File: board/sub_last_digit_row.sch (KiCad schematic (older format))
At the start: 55 parts, among them Q801 Q_PMOS_GSD, Q802 Q_PMOS_GSD, Q803 Q_PMOS_GSD, Q804 Q_PMOS_GSD, Q805 Q_PMOS_GSD, Q806 Q_PMOS_GSD, Q807 Q_PMOS_GSD, U801 TPIC6D595, U802 TPIC6D595, U803 TPIC6D595

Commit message: Almost all footprints done
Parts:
- D817, D818, D819: value (none) -> 14-segment; footprint (none) -> quokka:14-segment
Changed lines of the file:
@@
 P 5625 3275
 F 0 "D818" H 4825 3875 50  0000 L CNN
-F 1 " " H 4825 3875 50  0001 L CNN
-F 2 "" V 5225 2925 50  0001 C CNN
+F 1 "14-segment" H 4825 3875 50  0001 L CNN
+F 2 "quokka:14-segment" V 5225 2925 50  0001 C CNN
 F 3 "" V 5225 2925 50  0001 C CNN
 	1    5625 3275
@@
 P 7425 3275
 F 0 "D819" H 6625 3875 50  0000 L CNN
-F 1 " " H 6625 3875 50  0001 L CNN
-F 2 "" V 7025 2925 50  0001 C CNN
+F 1 "14-segment" H 6625 3875 50  0001 L CNN
+F 2 "quokka:14-segment" V 7025 2925 50  0001 C CNN
 F 3 "" V 7025 2925 50  0001 C CNN
 	1    7425 3275
@@
 P 3825 3275
 F 0 "D817" H 3025 3875 50  0000 L CNN
-F 1 " " H 3025 3875 50  0001 L CNN
-F 2 "" V 3425 2925 50  0001 C CNN
+F 1 "14-segment" H 3025 3875 50  0001 L CNN
+F 2 "quokka:14-segment" V 3425 2925 50  0001 C CNN
 F 3 "" V 3425 2925 50  0001 C CNN
 	1    3825 3275

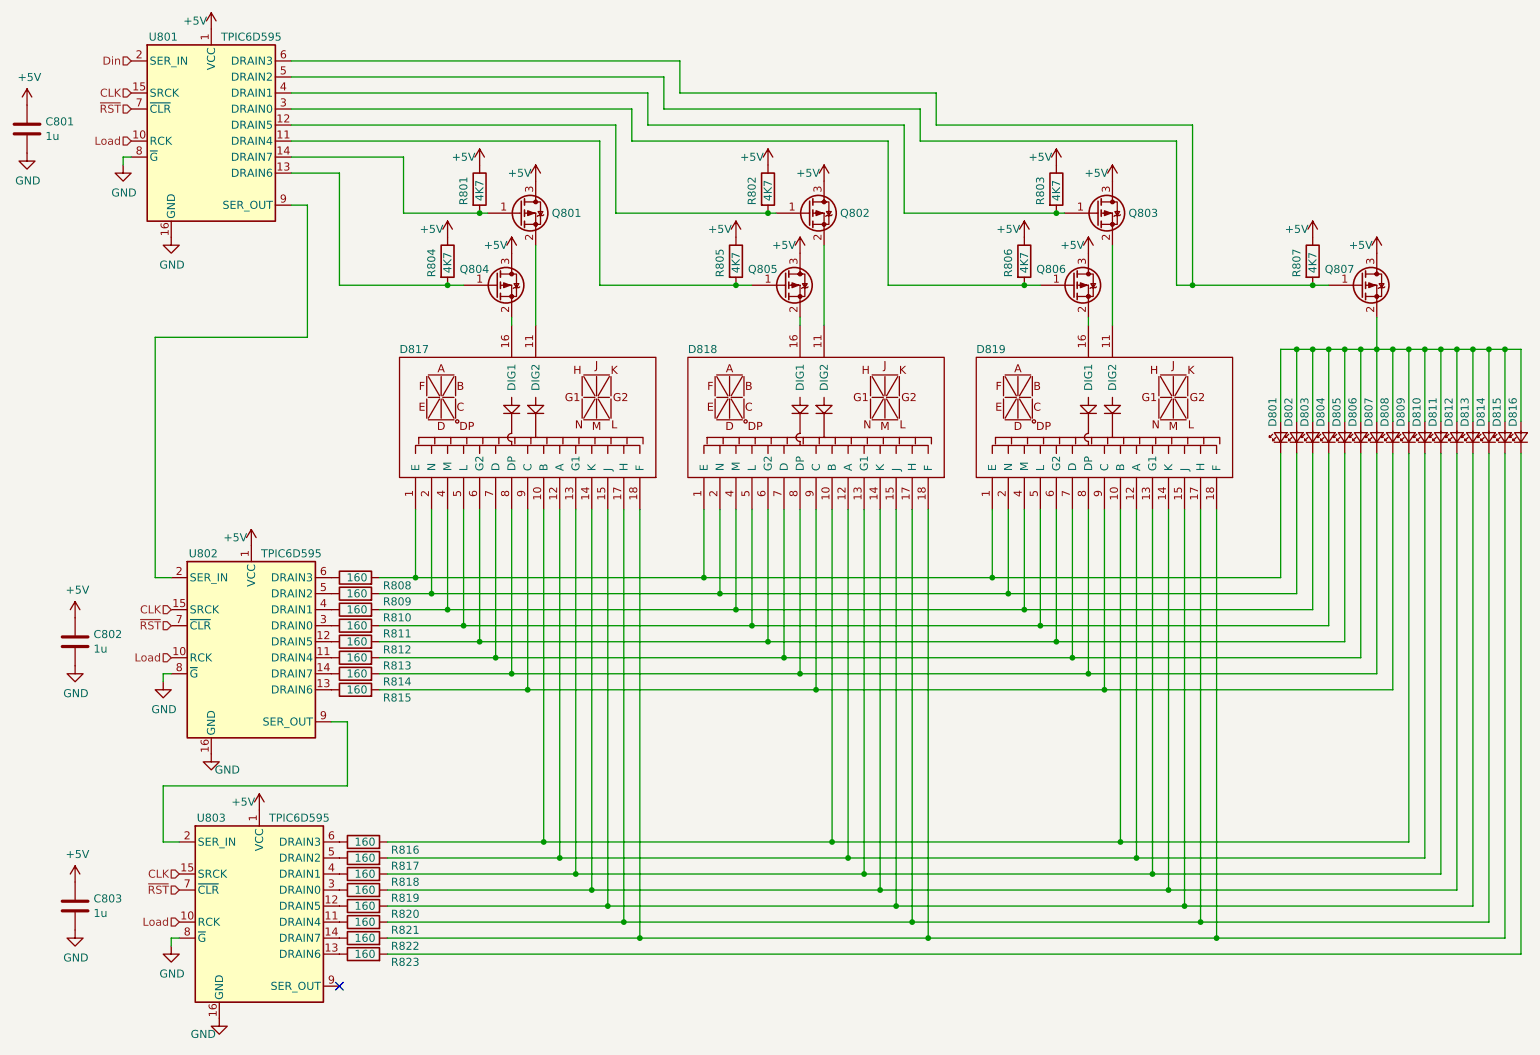
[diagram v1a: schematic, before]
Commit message: Power supply routed
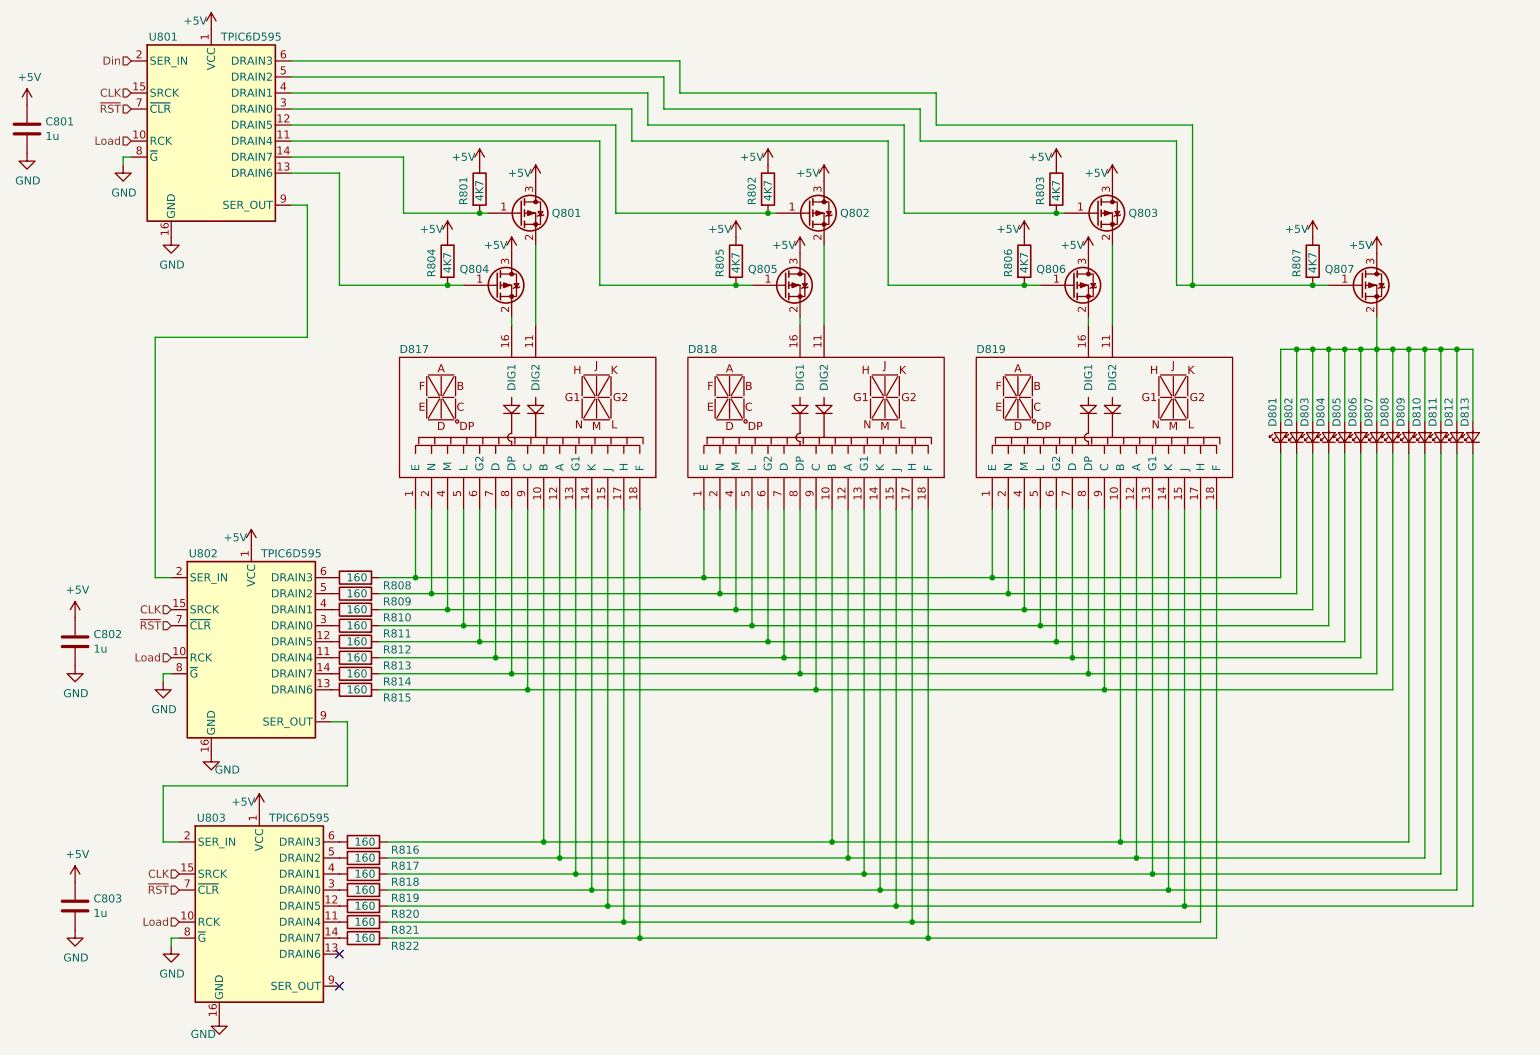
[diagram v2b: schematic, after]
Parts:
- removed D814, D815, D816: LED_Small, LED_SMD:LED_0805_2012Metric, symbol Device:LED_Small
- removed R823: 160, Resistor_SMD:R_1206_3216Metric, symbol Device:R
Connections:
- no-connect marks 1 -> 2
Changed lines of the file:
@@
 $EndComp
-Wire Wire Line
-	9925 2675 9925 3125
-Wire Wire Line
-	9825 2675 9925 2675
-Connection ~ 9825 2675
-Wire Wire Line
-	9825 2675 9825 3125
-Wire Wire Line
-	9725 2675 9825 2675
-Connection ~ 9725 2675
 Wire Wire Line
 	9725 2675 9725 3125
@@
 Wire Wire Line
 	8725 3125 8725 2675
-$Comp
-L Device:LED_Small D815
-U 1 1 5AF22EC2
-P 9925 3225
-F 0 "D815" H 10175 3275 50  0000 R CNN
-F 1 "LED_Small" V 9880 3157 50  0001 R CNN
-F 2 "LED_SMD:LED_0805_2012Metric" V 9925 3225 50  0001 C CNN
-F 3 "~" V 9925 3225 50  0001 C CNN
-	1    9925 3225
-	0    -1   -1   0
-$EndComp
-$Comp
-L Device:LED_Small D814
-U 1 1 5AF22EBC
-P 9825 3225
-F 0 "D814" H 10075 3275 50  0000 R CNN
-F 1 "LED_Small" V 9780 3157 50  0001 R CNN
-F 2 "LED_SMD:LED_0805_2012Metric" V 9825 3225 50  0001 C CNN
-F 3 "~" V 9825 3225 50  0001 C CNN
-	1    9825 3225
-	0    -1   -1   0
-$EndComp
 $Comp
 L Device:LED_Small D813
@@
 	0    -1   -1   0
 $EndComp
-$Comp
-L Device:LED_Small D816
-U 1 1 5AF22EC8
-P 10025 3225
-F 0 "D816" H 10275 3275 50  0000 R CNN
-F 1 "LED_Small" V 9980 3157 50  0001 R CNN
-F 2 "LED_SMD:LED_0805_2012Metric" V 10025 3225 50  0001 C CNN
-F 3 "~" V 10025 3225 50  0001 C CNN
-	1    10025 3225
-	0    -1   -1   0
-$EndComp
-Connection ~ 9925 2675
-Wire Wire Line
-	9925 2675 10025 2675
-Wire Wire Line
-	10025 2675 10025 3125
 Text HLabel 1350 875  0    50   Input ~ 0
 Din
@@
 Wire Wire Line
 	7925 6150 9725 6150
-Wire Wire Line
-	9825 6250 8025 6250
-Wire Wire Line
-	8125 6350 9925 6350
 Connection ~ 7525 5750
 Connection ~ 7625 5850
@@
 Connection ~ 7825 6050
 Connection ~ 7925 6150
-Connection ~ 8025 6250
-Connection ~ 8125 6350
 Wire Wire Line
 	2350 875  4775 875
@@
 	9725 3325 9725 6150
 Wire Wire Line
-	9825 3325 9825 6250
-Wire Wire Line
-	9925 3325 9925 6350
-Wire Wire Line
 	3825 3675 3825 4800
 Wire Wire Line
@@
 Wire Wire Line
 	7975 2275 8725 2275
-$Comp
-L Device:R R823
-U 1 1 5B0EC92D
-P 2800 6450
-F 0 "R823" V 2750 6100 50  0000 L CNN
-F 1 "160" V 2800 6375 50  0000 L CNN
-F 2 "Resistor_SMD:R_1206_3216Metric" V 2730 6450 50  0001 C CNN
-F 3 "~" H 2800 6450 50  0001 C CNN
-	1    2800 6450
-	0    -1   -1   0
-$EndComp
 NoConn ~ 2650 6650
-Wire Wire Line
-	2950 6450 10025 6450
-Wire Wire Line
-	10025 6450 10025 3325
+NoConn ~ 2650 6450
 $EndSCHEMATC
